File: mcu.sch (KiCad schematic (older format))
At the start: 51 parts, among them J11 RJ45_Shielded, J13 HR911105A, J2 RJ45_Shielded, U3 STM32F207VGT6, U4 MCP2562-E-P, U5 LAN8720A, Y1 Crystal_GND24

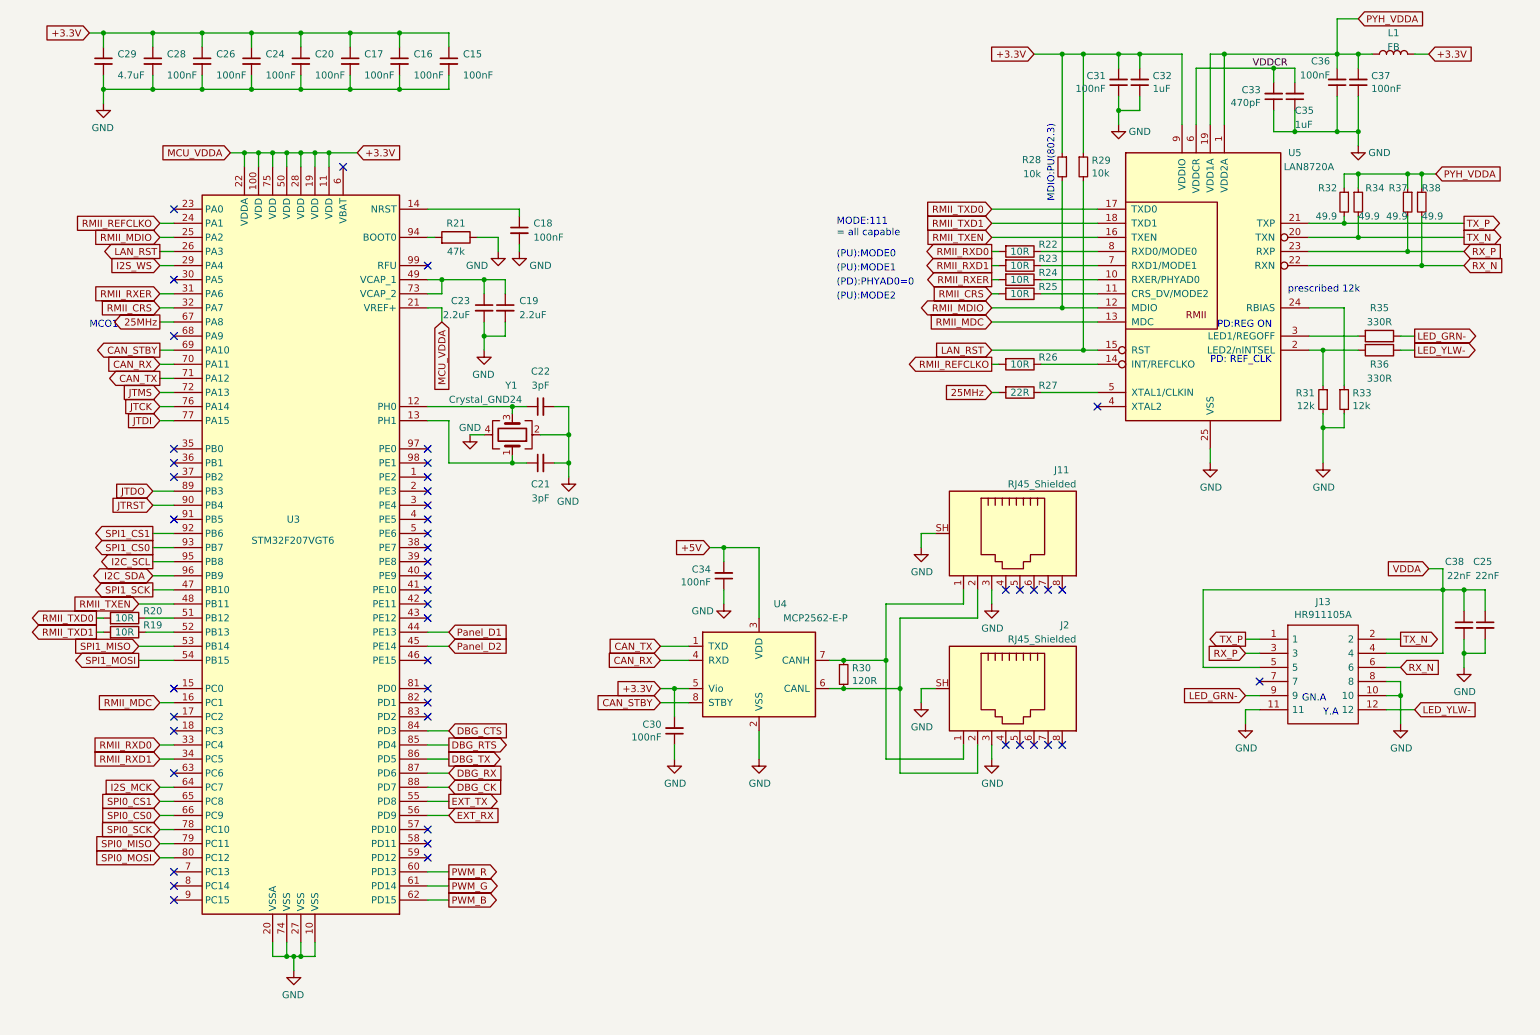
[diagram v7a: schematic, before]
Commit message: PHY routing done? Current sink routing is back to square one (yay fwd annotations)
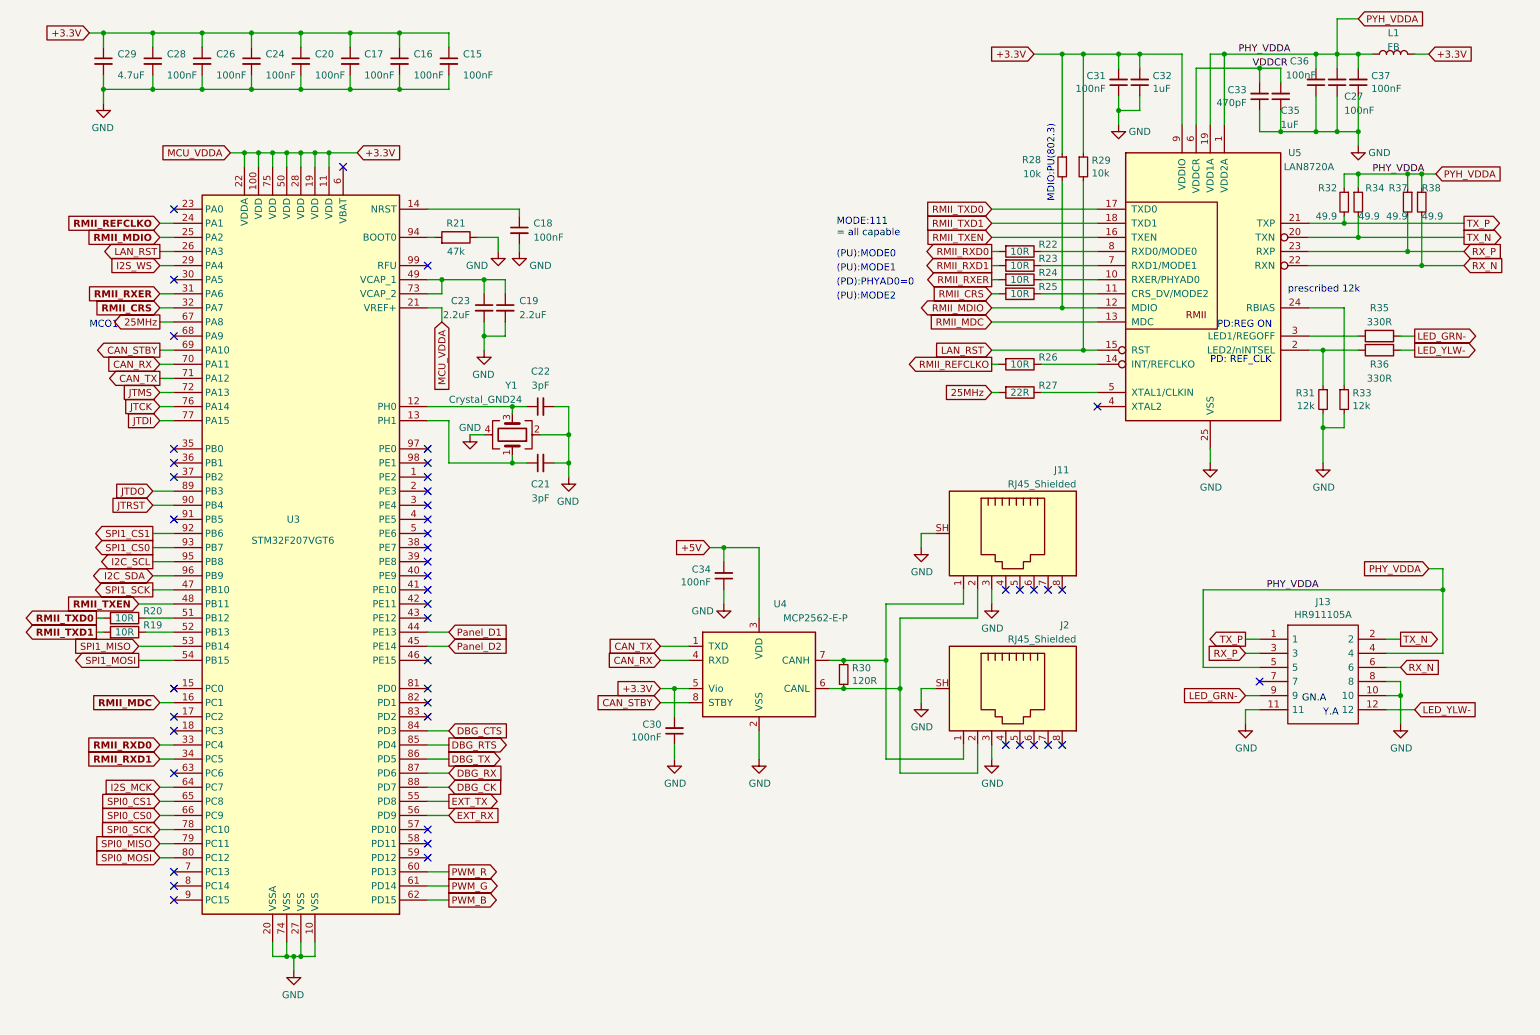
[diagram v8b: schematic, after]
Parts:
- removed C25, C38: 22nF, Capacitor_SMD:C_0603_1608Metric, symbol Device:C_Small
- added C27: 100nF, Capacitor_SMD:C_0603_1608Metric, symbol Device:C_Small
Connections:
- net VDDA is gone; now on net PHY_VDDA: J13.4, J13.5
- net GND: now also C27.1
- net PYH_VDDA renamed PHY_VDDA
- net PHY_VDDA: now also C27.2
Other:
- moved on the sheet: C33, C35
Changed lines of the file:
@@
 U 1 1 5BDB7E59
 P 9850 1100
-F 0 "C36" H 9800 950 50  0000 R CNN
-F 1 "100nF" H 9800 1050 50  0000 R CNN
+F 0 "C36" H 9650 950 50  0000 R CNN
+F 1 "100nF" H 9700 1050 50  0000 R CNN
 F 2 "Capacitor_SMD:C_0603_1608Metric" H 9850 1100 50  0001 C CNN
 F 3 "~" H 9850 1100 50  0001 C CNN
@@
 L Device:C_Small C35
 U 1 1 5BDE1B23
-P 9550 1200
-F 0 "C35" H 9550 1300 50  0000 R CNN
-F 1 "1uF" H 9550 1400 50  0000 R CNN
-F 2 "Capacitor_SMD:C_0603_1608Metric" H 9550 1200 50  0001 C CNN
-F 3 "~" H 9550 1200 50  0001 C CNN
-	1    9550 1200
+P 9450 1200
+F 0 "C35" H 9450 1300 50  0000 R CNN
+F 1 "1uF" H 9450 1400 50  0000 R CNN
+F 2 "Capacitor_SMD:C_0603_1608Metric" H 9450 1200 50  0001 C CNN
+F 3 "~" H 9450 1200 50  0001 C CNN
+	1    9450 1200
 	-1   0    0    1
 $EndComp
@@
 L Device:C_Small C33
 U 1 1 5BDE1B7D
-P 9400 1200
-F 0 "C33" H 9308 1154 50  0000 R CNN
-F 1 "470pF" H 9308 1245 50  0000 R CNN
-F 2 "Capacitor_SMD:C_0603_1608Metric" H 9400 1200 50  0001 C CNN
-F 3 "~" H 9400 1200 50  0001 C CNN
-	1    9400 1200
+P 9300 1200
+F 0 "C33" H 9208 1154 50  0000 R CNN
+F 1 "470pF" H 9208 1245 50  0000 R CNN
+F 2 "Capacitor_SMD:C_0603_1608Metric" H 9300 1200 50  0001 C CNN
+F 3 "~" H 9300 1200 50  0001 C CNN
+	1    9300 1200
 	1    0    0    1
 $EndComp
@@
 Text GLabel 9200 5450 0    50   Input ~ 0
 LED_GRN-
-$Comp
-L Device:C_Small C38
-U 1 1 5BF1D03C
-P 10750 4950
-F 0 "C38" H 10750 5400 50  0000 R CNN
-F 1 "22nF" H 10800 5300 50  0000 R CNN
-F 2 "Capacitor_SMD:C_0603_1608Metric" H 10750 4950 50  0001 C CNN
-F 3 "~" H 10750 4950 50  0001 C CNN
-	1    10750 4950
-	1    0    0    -1
-$EndComp
 Wire Wire Line
 	9300 5250 8900 5250
 Wire Wire Line
 	8900 4700 10600 4700
-$Comp
-L power:GND #PWR0108
-U 1 1 5BF30757
-P 10750 5250
-F 0 "#PWR0108" H 10750 5000 50  0001 C CNN
-F 1 "GND" H 10755 5077 50  0000 C CNN
-F 2 "" H 10750 5250 50  0001 C CNN
-F 3 "" H 10750 5250 50  0001 C CNN
-	1    10750 5250
-	1    0    0    -1
-$EndComp
 Text GLabel 10500 4550 0    50   Input ~ 0
-VDDA
+PHY_VDDA
 Wire Wire Line
 	10500 4550 10600 4550
 Wire Wire Line
 	10600 4550 10600 4700
-Connection ~ 10750 4700
 Text GLabel 10400 2900 2    50   Output ~ 0
 LED_GRN-
@@
 Wire Wire Line
 	1500 3300 1600 3300
-Text GLabel 1500 2100 0    50   Input ~ 0
+Text GLabel 1500 2100 0    50   Input ~ 10
 RMII_REFCLKO
-Text GLabel 1500 2700 0    50   Input ~ 0
+Text GLabel 1500 2700 0    50   Input ~ 10
 RMII_CRS
-Text GLabel 1500 5800 0    50   Input ~ 0
+Text GLabel 1500 5800 0    50   Input ~ 10
 RMII_RXD0
-Text GLabel 1500 5900 0    50   Input ~ 0
+Text GLabel 1500 5900 0    50   Input ~ 10
 RMII_RXD1
-Text GLabel 1350 4800 0    50   Input ~ 0
+Text GLabel 1350 4800 0    50   Input ~ 10
 RMII_TXEN
-Text GLabel 1050 4900 0    50   Output ~ 0
+Text GLabel 1050 4900 0    50   Output ~ 10
 RMII_TXD0
-Text GLabel 1050 5000 0    50   Output ~ 0
+Text GLabel 1050 5000 0    50   Output ~ 10
 RMII_TXD1
 Text GLabel 1500 2300 0    50   Output ~ 0
 LAN_RST
-Text GLabel 1500 2200 0    50   Input ~ 0
+Text GLabel 1500 2200 0    50   Input ~ 10
 RMII_MDIO
-Text GLabel 1500 5500 0    50   Input ~ 0
+Text GLabel 1500 5500 0    50   Input ~ 10
 RMII_MDC
-Text GLabel 1500 2600 0    50   Input ~ 0
+Text GLabel 1500 2600 0    50   Input ~ 10
 RMII_RXER
 Wire Wire Line
@@
 Wire Wire Line
 	10600 5150 10600 4700
-Wire Wire Line
-	10750 4700 10600 4700
-Wire Wire Line
-	10750 4700 10750 4850
-Wire Wire Line
-	10750 5050 10750 5150
 Connection ~ 10600 4700
 $Comp
@@
 	9850 1200 9850 1450
 Wire Wire Line
-	9550 1100 9550 1000
-Wire Wire Line
-	9550 1000 9400 1000
-Wire Wire Line
 	8850 1000 8850 1400
 Wire Wire Line
-	9400 1100 9400 1000
-Connection ~ 9400 1000
-Wire Wire Line
-	9400 1000 8850 1000
-Wire Wire Line
-	9050 900  9850 900
+	9050 900  9700 900
 Connection ~ 9050 900
-Wire Wire Line
-	9550 1300 9550 1450
-Wire Wire Line
-	9550 1450 9850 1450
 Connection ~ 9850 1450
 Wire Wire Line
-	9400 1300 9400 1450
-Wire Wire Line
-	9400 1450 9550 1450
-Connection ~ 9550 1450
+	9300 1300 9300 1450
 Text GLabel 10000 650  2    50   Input ~ 0
 PYH_VDDA
@@
 	10300 5450 10300 5650
 Connection ~ 10300 5450
-$Comp
-L Device:C_Small C25
-U 1 1 5E94BF88
-P 10900 4950
-F 0 "C25" H 10950 5400 50  0000 R CNN
-F 1 "22nF" H 11000 5300 50  0000 R CNN
-F 2 "Capacitor_SMD:C_0603_1608Metric" H 10900 4950 50  0001 C CNN
-F 3 "~" H 10900 4950 50  0001 C CNN
-	1    10900 4950
-	1    0    0    -1
-$EndComp
-Wire Wire Line
-	10900 5050 10900 5150
-Wire Wire Line
-	10900 5150 10750 5150
-Connection ~ 10750 5150
-Wire Wire Line
-	10750 5150 10750 5250
-Wire Wire Line
-	10900 4850 10900 4700
-Wire Wire Line
-	10900 4700 10750 4700
 Text Label 9250 1000 0    50   ~ 0
 VDDCR
+$Comp
+L Device:C_Small C27
+U 1 1 5BCFD8F3
+P 9700 1100
+F 0 "C27" H 9500 1200 50  0000 R CNN
+F 1 "100nF" H 9500 1300 50  0000 R CNN
+F 2 "Capacitor_SMD:C_0603_1608Metric" H 9700 1100 50  0001 C CNN
+F 3 "~" H 9700 1100 50  0001 C CNN
+	1    9700 1100
+	-1   0    0    1
+$EndComp
+Wire Wire Line
+	9700 1000 9700 900
+Connection ~ 9700 900
+Wire Wire Line
+	9700 900  9850 900
+Wire Wire Line
+	9700 1200 9700 1450
+Connection ~ 9700 1450
+Wire Wire Line
+	9700 1450 9850 1450
+Wire Wire Line
+	9300 1450 9450 1450
+Wire Wire Line
+	9450 1300 9450 1450
+Connection ~ 9450 1450
+Wire Wire Line
+	9450 1450 9700 1450
+Wire Wire Line
+	8850 1000 9300 1000
+Wire Wire Line
+	9450 1000 9450 1100
+Wire Wire Line
+	9300 1100 9300 1000
+Connection ~ 9300 1000
+Wire Wire Line
+	9300 1000 9450 1000
+Text Label 9150 900  0    50   ~ 0
+PHY_VDDA
+Text Label 10100 1750 0    50   ~ 0
+PHY_VDDA
+Text Label 9350 4700 0    50   ~ 0
+PHY_VDDA
 $EndSCHEMATC
